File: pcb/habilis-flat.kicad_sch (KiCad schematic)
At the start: 74 parts, among them J1 AudioJack4, J2 AudioJack4, SW1 MX, SW10 MX, SW11 MX, SW12 MX, SW13 MX, SW14 MX, SW15 MX, SW16 MX, SW17 MX, SW18 MX, SW19 MX, SW2 MX, SW20 MX, SW21 MX, SW22 MX, SW23 MX, SW24 MX, SW25 MX, SW26 MX, SW27 MX, SW28 MX, SW29 MX, SW3 MX, SW30 MX, SW31 MX, SW32 MX, SW33 MX, SW34 MX, SW35 MX, SW4 MX, SW5 MX, SW6 MX, SW7 MX, SW8 MX, SW9 MX, U1 ProMicro

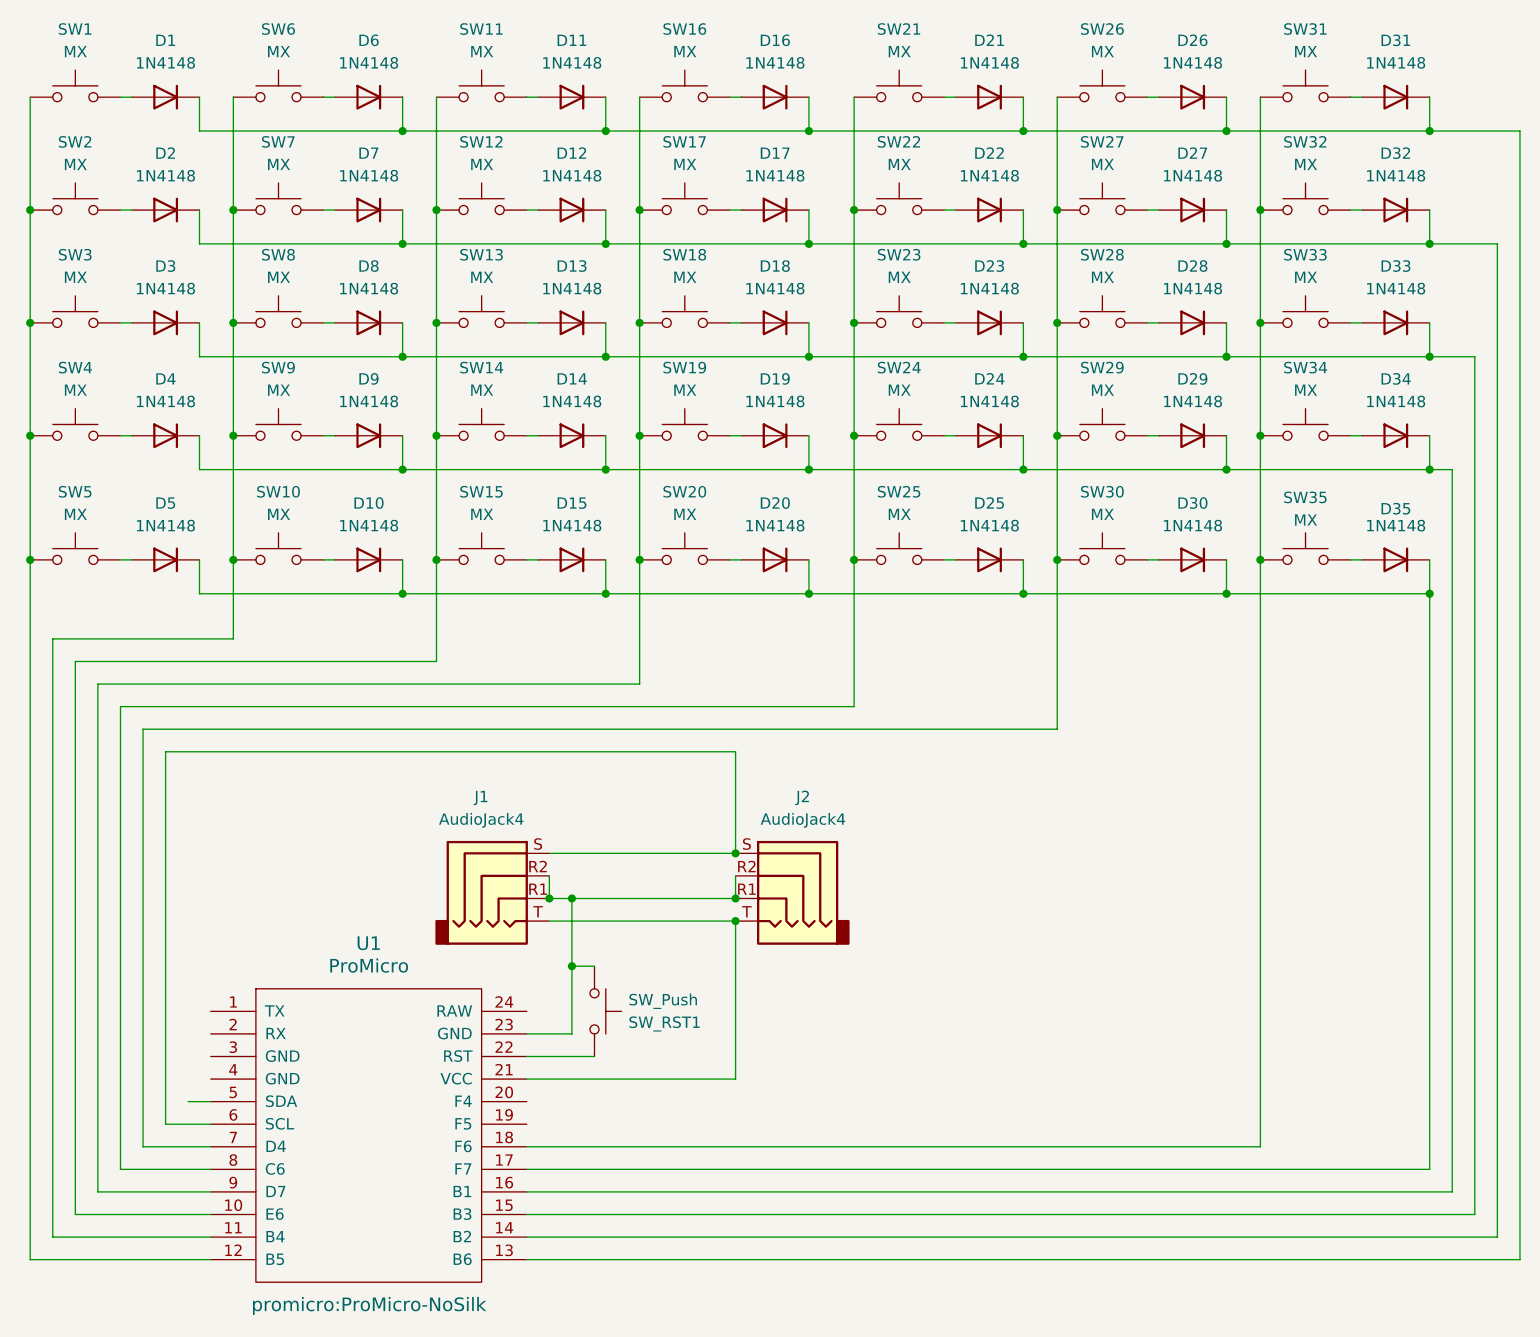
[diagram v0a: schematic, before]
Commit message: Simplify schematic, update diode footprint reference
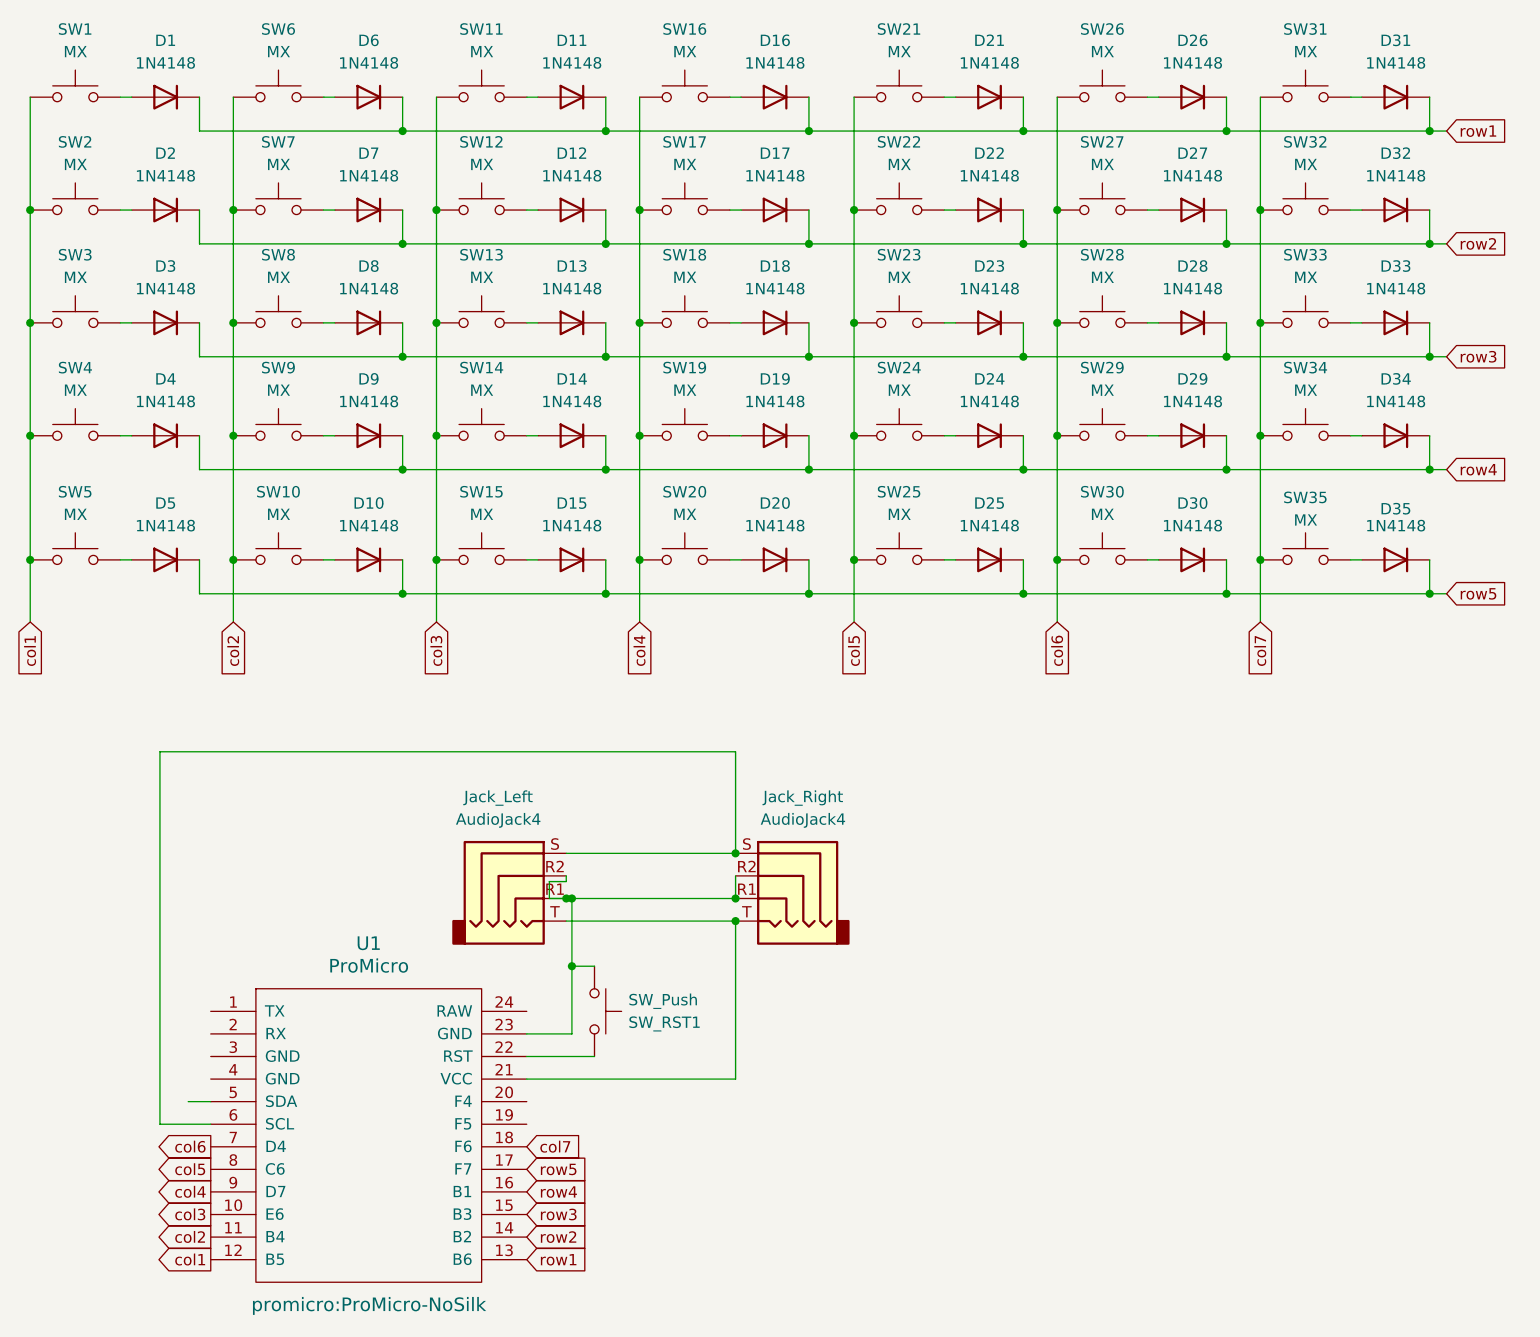
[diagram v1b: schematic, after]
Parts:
- D1, D10, D11, D12, D13, D14, D15, D16, D17, D18, D19, D2, D20, D21, D22, D23, D24, D25, D26, D27, D28, D29, D3, D30, D31, D32, D33, D34, D35, D4, D5, D6, D7, D8, D9: footprint Diode_THT:D_DO-35_SOD27_P7.62mm_Horizontal -> project-components:D_DO-35_SOD27_P7.62mm_Horizontal
- renumbered J1 to Jack_Left, J2 to Jack_Right
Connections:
- net row4: now reaches D14.1 (K), D19.1 (K), D24.1 (K), D29.1 (K), D34.1 (K), D4.1 (K), D9.1 (K), U1.16 (B1)
- net col1: now reaches SW1.2, SW2.2, SW3.2, SW4.2, SW5.2, U1.12 (B5)
- net row5: now reaches D10.1 (K), D15.1 (K), D20.1 (K), D25.1 (K), D30.1 (K), D35.1 (K), D5.1 (K), U1.17 (F7)
- net col5: now reaches SW21.2, SW22.2, SW23.2, SW24.2, SW25.2, U1.8 (C6)
- net col6: now reaches SW26.2, SW27.2, SW28.2, SW29.2, SW30.2, U1.7 (D4)
- net row1: now reaches D1.1 (K), D11.1 (K), D16.1 (K), D21.1 (K), D26.1 (K), D31.1 (K), D6.1 (K), U1.13 (B6)
- net col7: now reaches SW31.2, SW32.2, SW33.1, SW34.2, SW35.2, U1.18 (F6)
- net row2: now reaches D12.1 (K), D17.1 (K), D2.1 (K), D22.1 (K), D27.1 (K), D32.1 (K), D7.1 (K), U1.14 (B2)
- net col4: now reaches SW16.2, SW17.2, SW18.2, SW19.2, SW20.2, U1.9 (D7)
- net row3: now reaches D13.1 (K), D18.1 (K), D23.1 (K), D28.1 (K), D3.1 (K), D33.1 (K), D8.1 (K), U1.15 (B3)
- net col2: now reaches SW10.2, SW6.2, SW7.2, SW8.2, SW9.2, U1.11 (B4)
- net col3: now reaches SW11.2, SW12.2, SW13.2, SW14.2, SW15.2, U1.10 (E6)
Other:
- moved on the sheet: Jack_Left
